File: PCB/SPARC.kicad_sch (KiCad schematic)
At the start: 88 parts, among them J1 Conn_Coaxial_Power, J2 Conn_Coaxial_Power, J3 Conn_01x06_Female, J4 Conn_01x03_Female, J5 Conn_01x03_Female, J6 Conn_01x06_Female, U1 HV2621, U2 HV2621

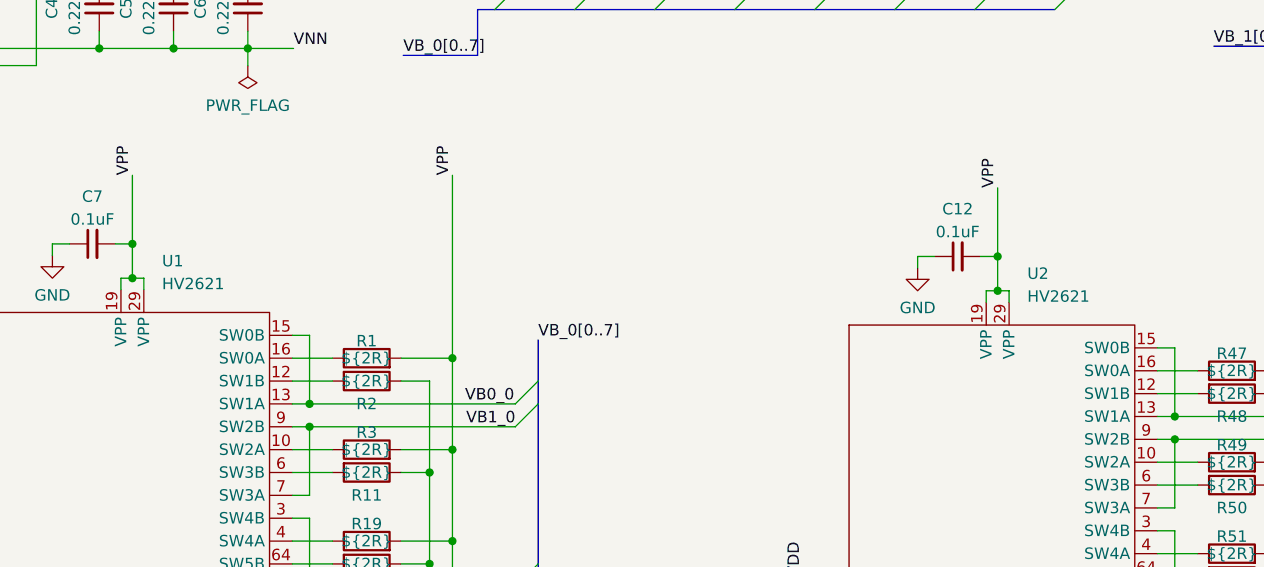
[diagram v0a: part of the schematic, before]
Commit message: Changed silkscreen
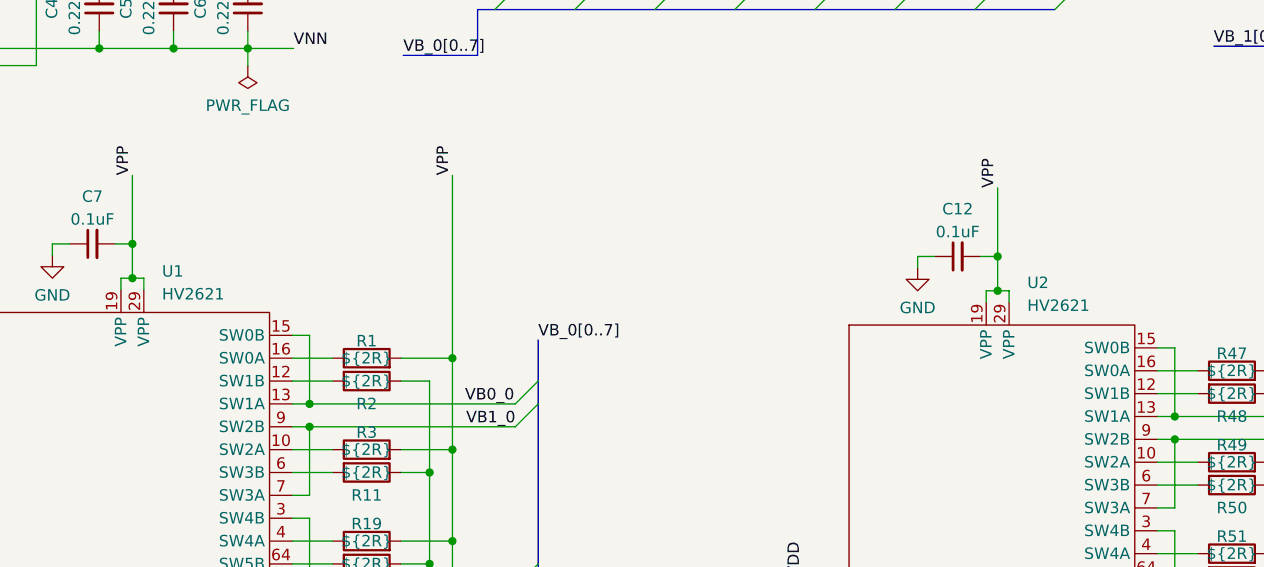
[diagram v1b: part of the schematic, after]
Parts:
- U1, U2: footprint Package_DFN_QFN:VQFN-64-1EP_9x9mm_P0.5mm_EP7.15x7.15mm_ThermalVias -> grad_kicad_foot:VQFN-64-1EP_9x9mm_P0.5mm_EP7.15x7.15mm_ThermalVias_0.25mm
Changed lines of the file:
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@@
   (symbol (lib_id "grad:HV2621") (at 60.198 113.792 0) (unit 1)
     (in_bom yes) (on_board yes) (fields_autoplaced)
-    (property "Reference" "U1" (id 0) (at 64.7574 67.437 0)
+    (property "Reference" "U1" (id 0) (at 64.7574 68.58 0)
       (effects (font (size 1.27 1.27)) (justify left))
     )
-    (property "Value" "HV2621" (id 1) (at 64.7574 69.977 0)
+    (property "Value" "HV2621" (id 1) (at 64.7574 71.12 0)
       (effects (font (size 1.27 1.27)) (justify left))
     )
-    (property "Footprint" "Package_DFN_QFN:VQFN-64-1EP_9x9mm_P0.5mm_EP7.15x7.15mm_ThermalVias" (id 2) (at 66.548 113.792 90)
+    (property "Footprint" "grad_kicad_foot:VQFN-64-1EP_9x9mm_P0.5mm_EP7.15x7.15mm_ThermalVias_0.25mm" (id 2) (at 66.548 113.792 90)
       (effects (font (size 1.27 1.27)) hide)
     )
@@
   (symbol (lib_id "grad:HV2621") (at 156.337 115.189 0) (unit 1)
     (in_bom yes) (on_board yes) (fields_autoplaced)
-    (property "Reference" "U2" (id 0) (at 160.8964 68.834 0)
+    (property "Reference" "U2" (id 0) (at 160.8964 69.85 0)
       (effects (font (size 1.27 1.27)) (justify left))
     )
-    (property "Value" "HV2621" (id 1) (at 160.8964 71.374 0)
+    (property "Value" "HV2621" (id 1) (at 160.8964 72.39 0)
       (effects (font (size 1.27 1.27)) (justify left))
     )
-    (property "Footprint" "Package_DFN_QFN:VQFN-64-1EP_9x9mm_P0.5mm_EP7.15x7.15mm_ThermalVias" (id 2) (at 162.687 115.189 90)
+    (property "Footprint" "grad_kicad_foot:VQFN-64-1EP_9x9mm_P0.5mm_EP7.15x7.15mm_ThermalVias_0.25mm" (id 2) (at 162.687 115.189 90)
       (effects (font (size 1.27 1.27)) hide)
     )
@@
     )
     (path "/28c1d54b-da16-4414-b15f-48fa4c2ed610"
-      (reference "U1") (unit 1) (value "HV2621") (footprint "Package_DFN_QFN:VQFN-64-1EP_9x9mm_P0.5mm_EP7.15x7.15mm_ThermalVias")
+      (reference "U1") (unit 1) (value "HV2621") (footprint "grad_kicad_foot:VQFN-64-1EP_9x9mm_P0.5mm_EP7.15x7.15mm_ThermalVias_0.25mm")
     )
     (path "/6cfd335e-3366-4636-ad0e-f1fe5cc98c25"
-      (reference "U2") (unit 1) (value "HV2621") (footprint "Package_DFN_QFN:VQFN-64-1EP_9x9mm_P0.5mm_EP7.15x7.15mm_ThermalVias")
-    )
-  )
+      (reference "U2") (unit 1) (value "HV2621") (footprint "grad_kicad_foot:VQFN-64-1EP_9x9mm_P0.5mm_EP7.15x7.15mm_ThermalVias_0.25mm")
+    )
+  )
